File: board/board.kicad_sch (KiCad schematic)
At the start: 4 parts, among them J1 012_CAN, J2 Conn_01x03_Male

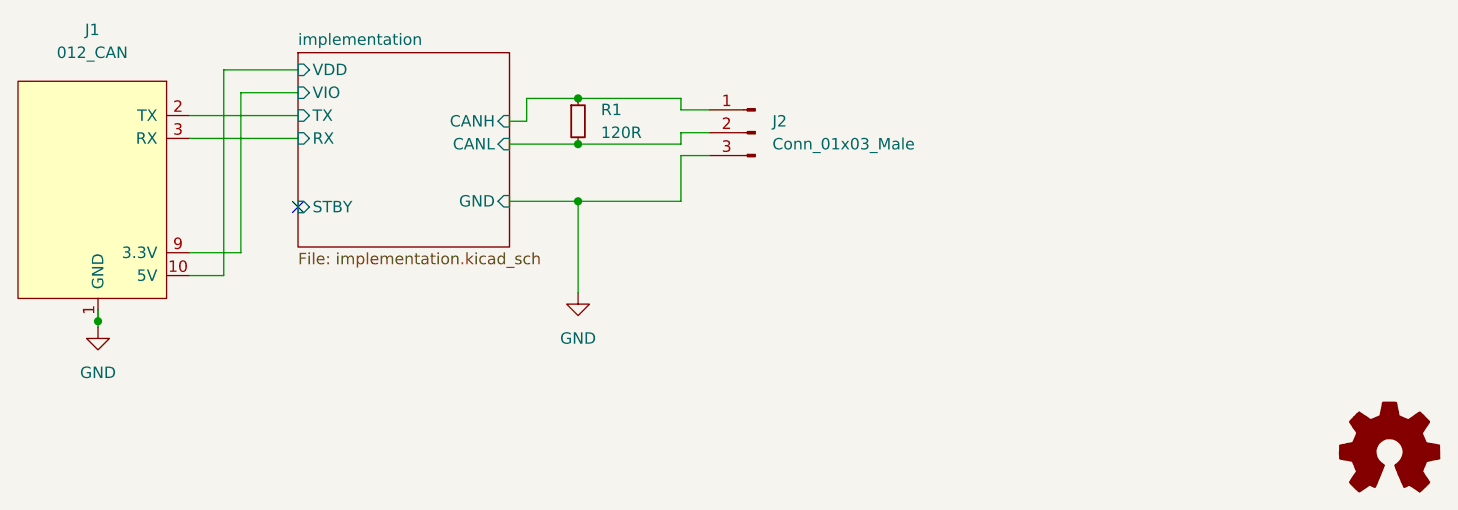
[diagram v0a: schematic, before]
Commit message: renamed subsheet to work better in compositions
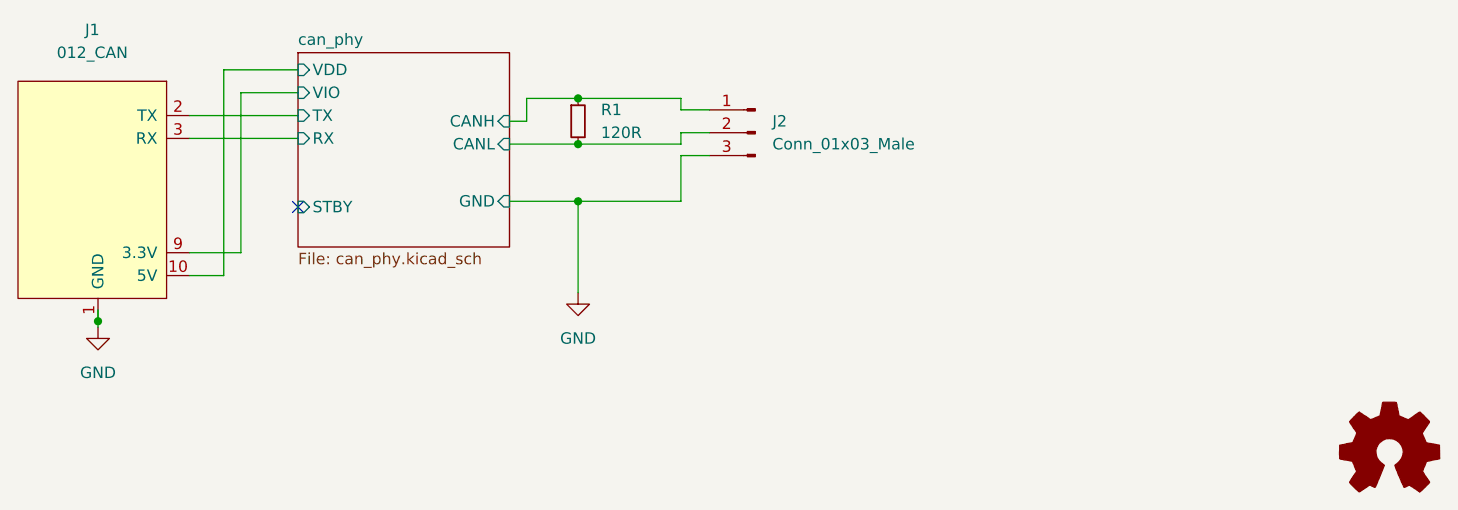
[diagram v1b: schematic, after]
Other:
- sheet implementation renamed can_phy
- sheet can_phy: file implementation.kicad_sch -> can_phy.kicad_sch
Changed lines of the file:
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@@
     (stroke (width 0.1524) (type solid) (color 0 0 0 0))
     (fill (color 0 0 0 0.0000))
-    (property "Sheet name" "implementation" (id 0) (at 151.765 112.3184 0)
+    (property "Sheet name" "can_phy" (id 0) (at 151.765 112.3184 0)
       (effects (font (size 1.27 1.27)) (justify left bottom))
     )
-    (property "Sheet file" "implementation.kicad_sch" (id 1) (at 151.765 135.2046 0)
+    (property "Sheet file" "can_phy.kicad_sch" (id 1) (at 151.765 135.2046 0)
       (effects (font (size 1.27 1.27)) (justify left top))
     )
